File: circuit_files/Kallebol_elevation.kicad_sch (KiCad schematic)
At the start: 31 parts

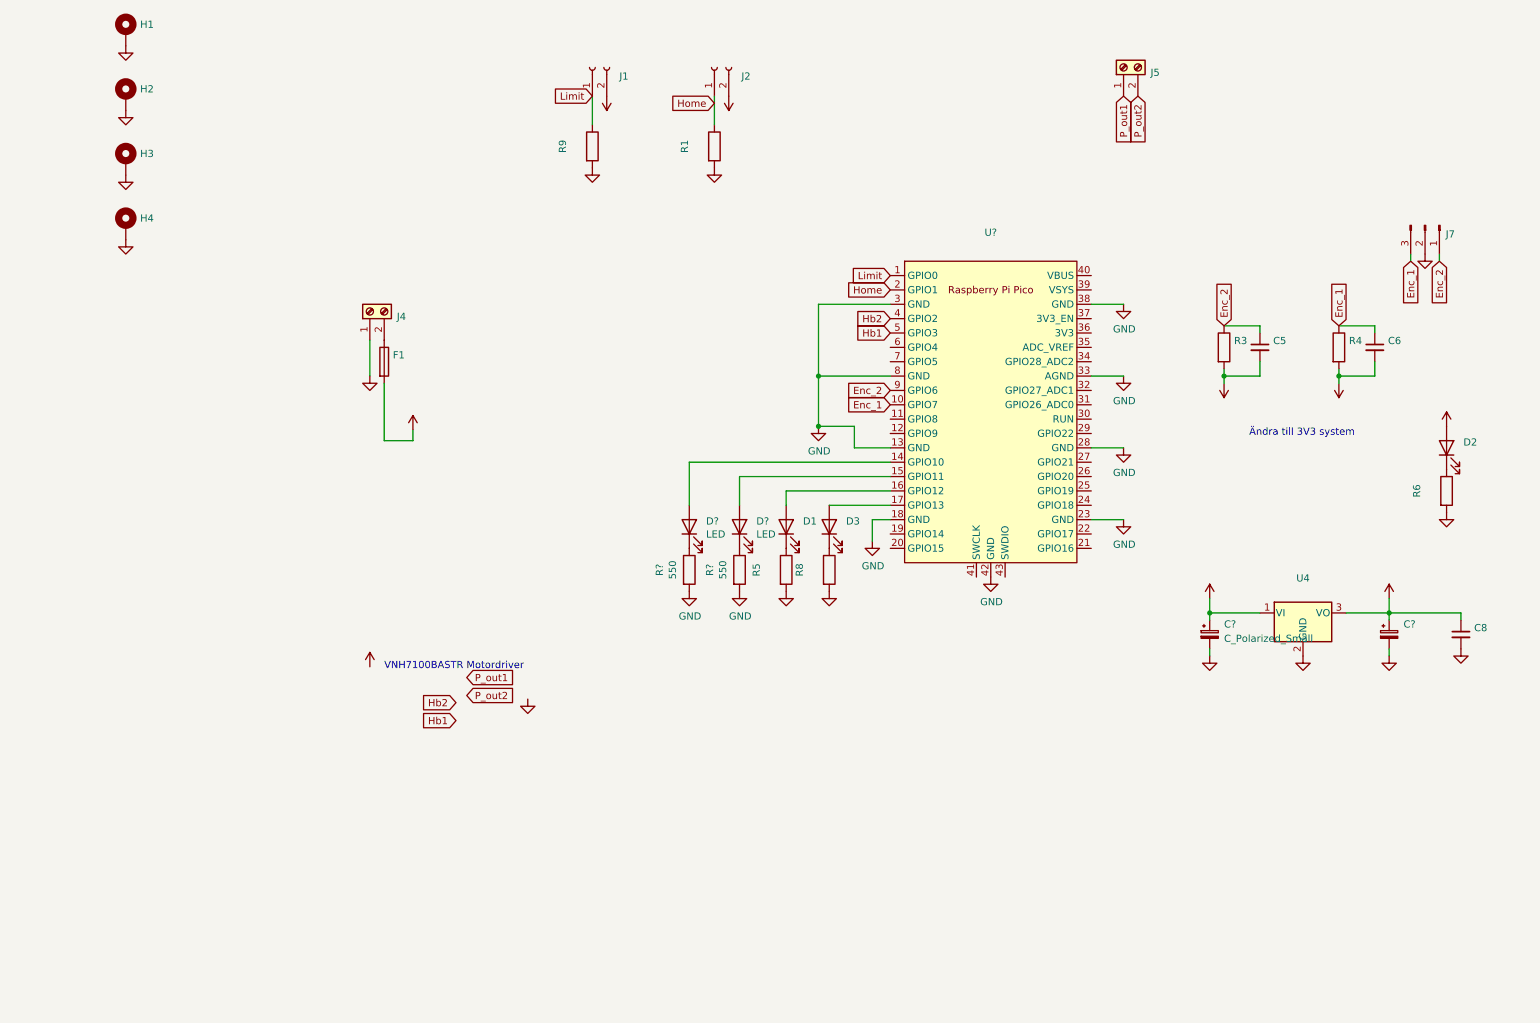
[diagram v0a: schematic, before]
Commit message: added basic driver circuit
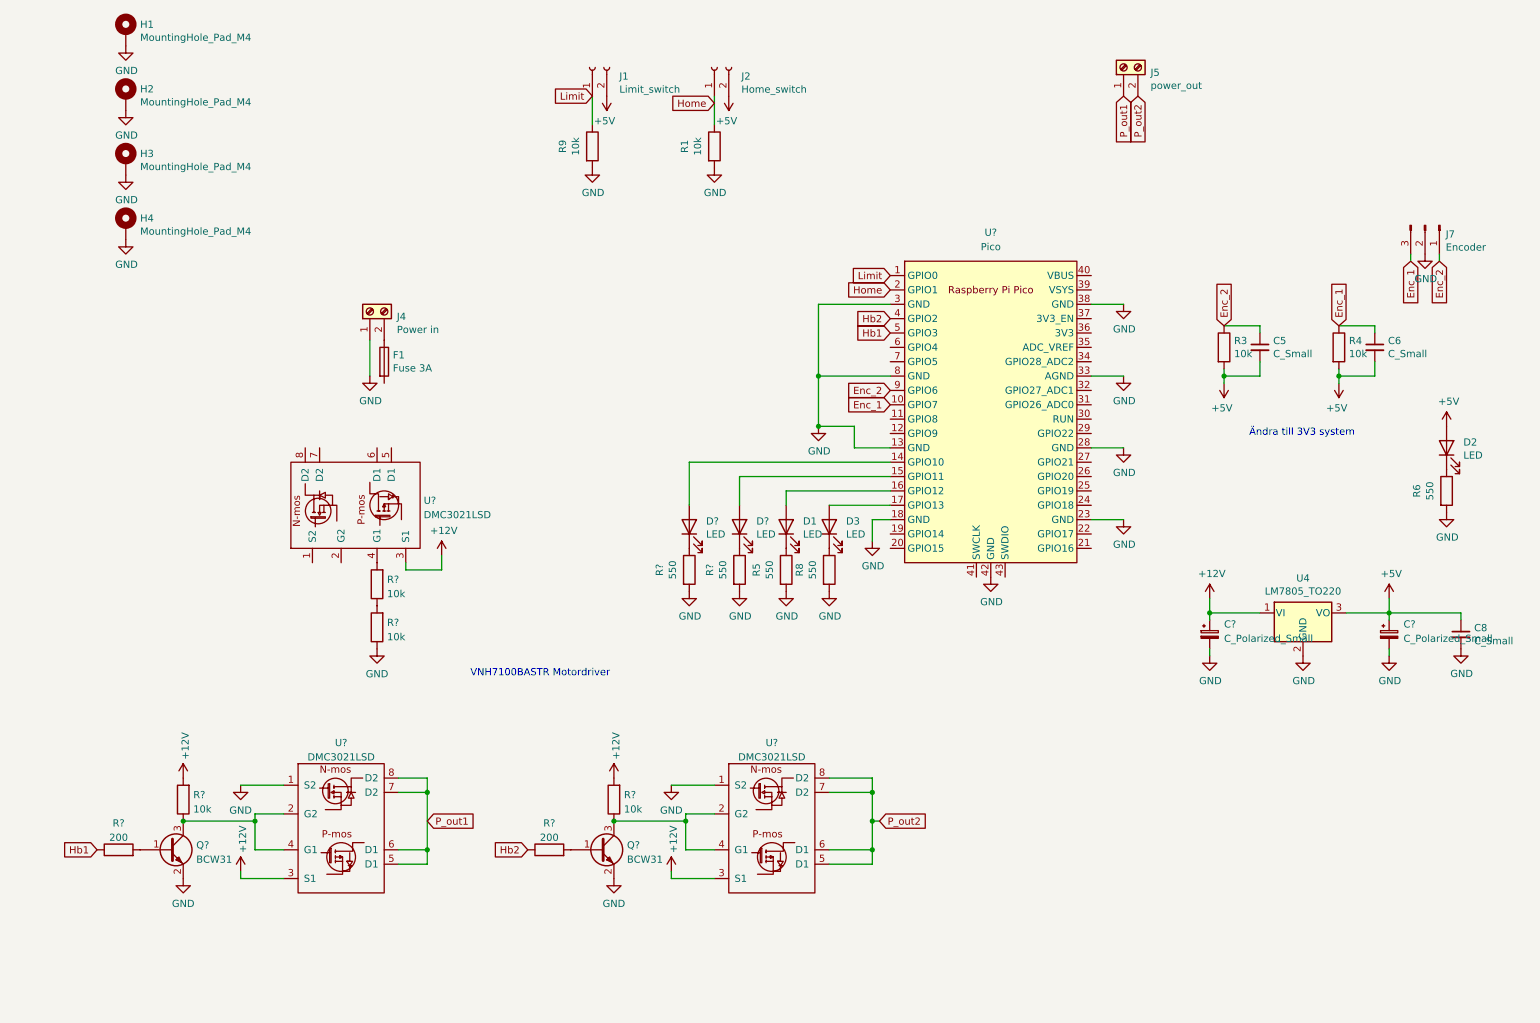
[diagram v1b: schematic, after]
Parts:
- added Q? (x2): BCW31, symbol Device:Q_NPN_BEC
- added R? (x2): 200, symbol Device:R
- added R? (x4): 10k, symbol Device:R
- added U? (x3): DMC3021LSD, Package_SO:SOIC-8_3.9x4.9mm_P1.27mm, symbol Kallebol_symLib:DMC3021LSD
- C5, C6, C8: value (none) -> C_Small; footprint (none) -> Capacitor_SMD:C_0603_1608Metric_Pad1.05x0.95mm_HandSolder
- C?: value (none) -> C_Polarized_Small
- D1, D2, D3: value (none) -> LED; footprint (none) -> LED_SMD:LED_0603_1608Metric
- F1: value (none) -> Fuse 3A; footprint (none) -> Xp_motor:Fuse_holder
- H1, H2, H3, H4: value (none) -> MountingHole_Pad_M4; footprint (none) -> MountingHole:MountingHole_4.3mm_M4_Pad
- J1: value (none) -> Limit_switch; footprint (none) -> TerminalBlock:TerminalBlock_bornier-2_P5.08mm
- J2: value (none) -> Home_switch; footprint (none) -> TerminalBlock:TerminalBlock_bornier-2_P5.08mm
- J4: value (none) -> Power in; footprint (none) -> TerminalBlock:TerminalBlock_bornier-2_P5.08mm
- J5: value (none) -> power_out; footprint (none) -> TerminalBlock:TerminalBlock_bornier-2_P5.08mm
- J7: value (none) -> Encoder; footprint (none) -> Connector_PinSocket_2.54mm:PinSocket_1x03_P2.54mm_Vertical
- R1, R3, R4, R9: value (none) -> 10k; footprint (none) -> Resistor_SMD:R_0603_1608Metric_Pad1.05x0.95mm_HandSolder
- R5, R6, R8: value (none) -> 550; footprint (none) -> Resistor_SMD:R_0603_1608Metric_Pad1.05x0.95mm_HandSolder
- U4: value (none) -> LM7805_TO220; footprint (none) -> Package_TO_SOT_THT:TO-220-3_Vertical
- U?: value (none) -> Pico; footprint (none) -> RPi_Pico:RPi_Pico_SMD_TH
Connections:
- net +12V: now also R?.2, R?.2, U?.3 (S1), U?.3 (S1), U?.3 (S1); no longer F1.2
- net GND: now also Q?.2 (E), Q?.2 (E), R?.1, U?.1 (S2), U?.1 (S2)
- net Hb1: now also R?.1
- net Hb2: now also R?.1
- net P_out1: now also U?.5 (D1), U?.6 (D1), U?.7 (D2), U?.8 (D2)
- net P_out2: now also U?.5 (D1), U?.6 (D1), U?.7 (D2), U?.8 (D2)
- new net: Q?.1 (B), R?.2 (x2)
- new net: Q?.3 (C), R?.1, U?.2 (G2), U?.4 (G1) (x2)
- new net: R?.1, R?.2
- new net: R?.2, U?.4 (G1)

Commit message: elevation part of the board functional
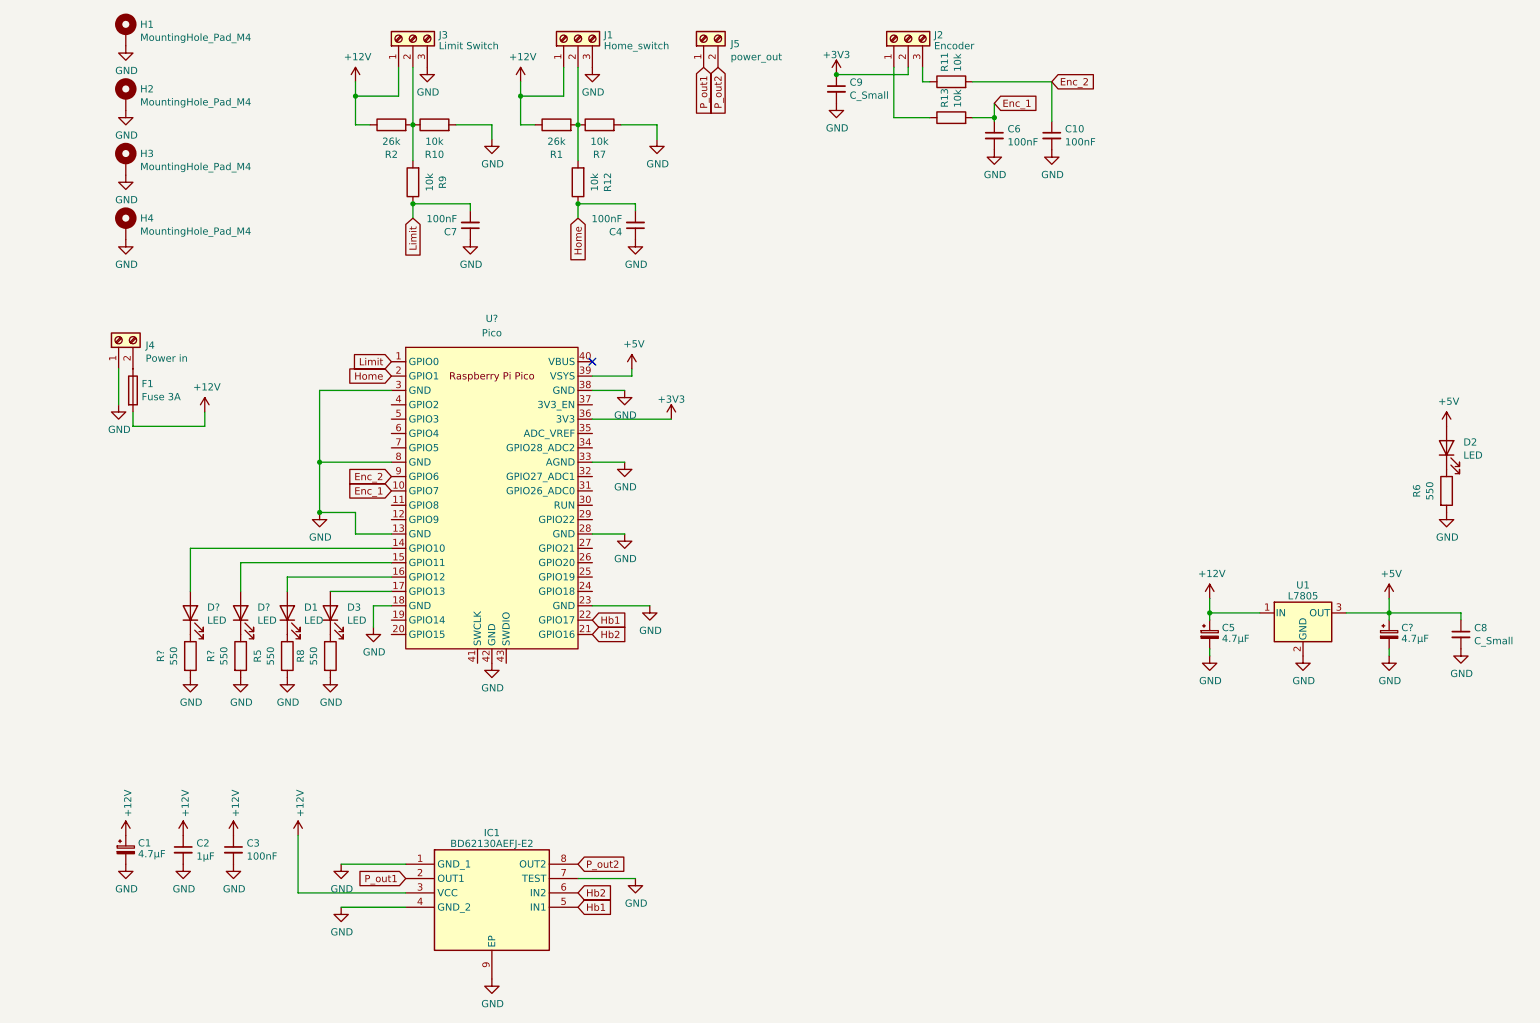
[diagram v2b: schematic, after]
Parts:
- removed C5: C_Small, Capacitor_SMD:C_0603_1608Metric_Pad1.05x0.95mm_HandSolder, symbol Device:C_Small
- removed C?: C_Polarized_Small, symbol Device:C_Polarized_Small
- removed J1: Limit_switch, TerminalBlock:TerminalBlock_bornier-2_P5.08mm, symbol Connector:Conn_01x02_Female
- removed J2: Home_switch, TerminalBlock:TerminalBlock_bornier-2_P5.08mm, symbol Connector:Conn_01x02_Female
- removed J7: Encoder, Connector_PinSocket_2.54mm:PinSocket_1x03_P2.54mm_Vertical, symbol Connector:Conn_01x03_Male
- removed Q? (x2): BCW31, symbol Device:Q_NPN_BEC
- removed R3, R4: 10k, Resistor_SMD:R_0603_1608Metric_Pad1.05x0.95mm_HandSolder, symbol Device:R
- removed R? (x2): 200, symbol Device:R
- removed R? (x4): 10k, symbol Device:R
- removed U4: LM7805_TO220, Package_TO_SOT_THT:TO-220-3_Vertical, symbol Regulator_Linear:LM7805_TO220
- removed U? (x3): DMC3021LSD, Package_SO:SOIC-8_3.9x4.9mm_P1.27mm, symbol Kallebol_symLib:DMC3021LSD
- added C1, C5: 4.7µF, symbol Device:C_Polarized_Small
- added C10, C3, C4, C7: 100nF, Capacitor_SMD:C_0603_1608Metric_Pad1.05x0.95mm_HandSolder, symbol Device:C_Small
- added C2: 1µF, Capacitor_SMD:C_0603_1608Metric_Pad1.05x0.95mm_HandSolder, symbol Device:C_Small
- added C9: C_Small, Capacitor_SMD:C_0603_1608Metric_Pad1.05x0.95mm_HandSolder, symbol Device:C_Small
- added IC1: BD62130AEFJ-E2, SOIC127P600X100-9N, symbol BD62130AEFJ-E2:BD62130AEFJ-E2
- added J1: Home_switch, symbol Connector:Screw_Terminal_01x03
- added J2: Encoder, symbol Connector:Screw_Terminal_01x03
- added J3: Limit Switch, symbol Connector:Screw_Terminal_01x03
- added R10, R11, R12, R13, R7: 10k, Resistor_SMD:R_0603_1608Metric_Pad1.05x0.95mm_HandSolder, symbol Device:R
- added R2: 26k, Resistor_SMD:R_0603_1608Metric_Pad1.05x0.95mm_HandSolder, symbol Device:R
- added U1: L7805, symbol Regulator_Linear:L7805
- C6: value C_Small -> 100nF
- C?: value C_Polarized_Small -> 4.7µF
- R1: value 10k -> 26k
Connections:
- net +12V: now also F1.2, R1.1, C1.1, C2.1, C3.1, C5.1, IC1.3 (VCC), J1.1 (Pin_1), J3.1 (Pin_1), R2.1, U1.1 (IN)
- net +5V: now also U?.39 (VSYS), U1.3 (OUT); no longer C6.2
- net Enc_1: now also R13.2
- net Enc_2: now also C10.1, R11.2
- net GND: now also C6.2, C1.2, C10.2, C2.2, C3.2, C4.1, C5.2, C7.1, C9.2, IC1.1 (GND_1), IC1.4 (GND_2), IC1.7 (TEST), IC1.9 (EP), J1.3 (Pin_3), J3.3 (Pin_3), R10.2, R7.2, U1.2 (GND); no longer R1.2, R9.2
- net Hb1: now also U?.22 (GPIO17), IC1.5 (IN1); no longer U?.5 (GPIO3)
- net Hb2: now also U?.21 (GPIO16), IC1.6 (IN2); no longer U?.4 (GPIO2)
- net Home: now also C4.2, R12.1; no longer R1.1
- net Limit: now also C7.2
- net P_out1: now also IC1.2 (OUT1)
- net P_out2: now also IC1.8 (OUT2)
- net +3V3: now reaches U?.36 (3V3)
- net +3V3: now also C9.1, J2.2 (Pin_2)
- new net: J2.1 (Pin_1), R13.1
- new net: J3.2 (Pin_2), R10.1, R2.2, R9.2
- new net: J2.3 (Pin_3), R11.1
- new net: J1.2 (Pin_2), R1.2, R12.2, R7.1
- no-connect marks 0 -> 1
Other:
- note removed: "VNH7100BASTR Motordriver"
- note removed: "Ändra till 3V3 system"
- moved on the sheet: D1, D3, D?, F1, J4, J5, R5, R8, R?, U?

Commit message: merged functionality with the GPIO fanout board
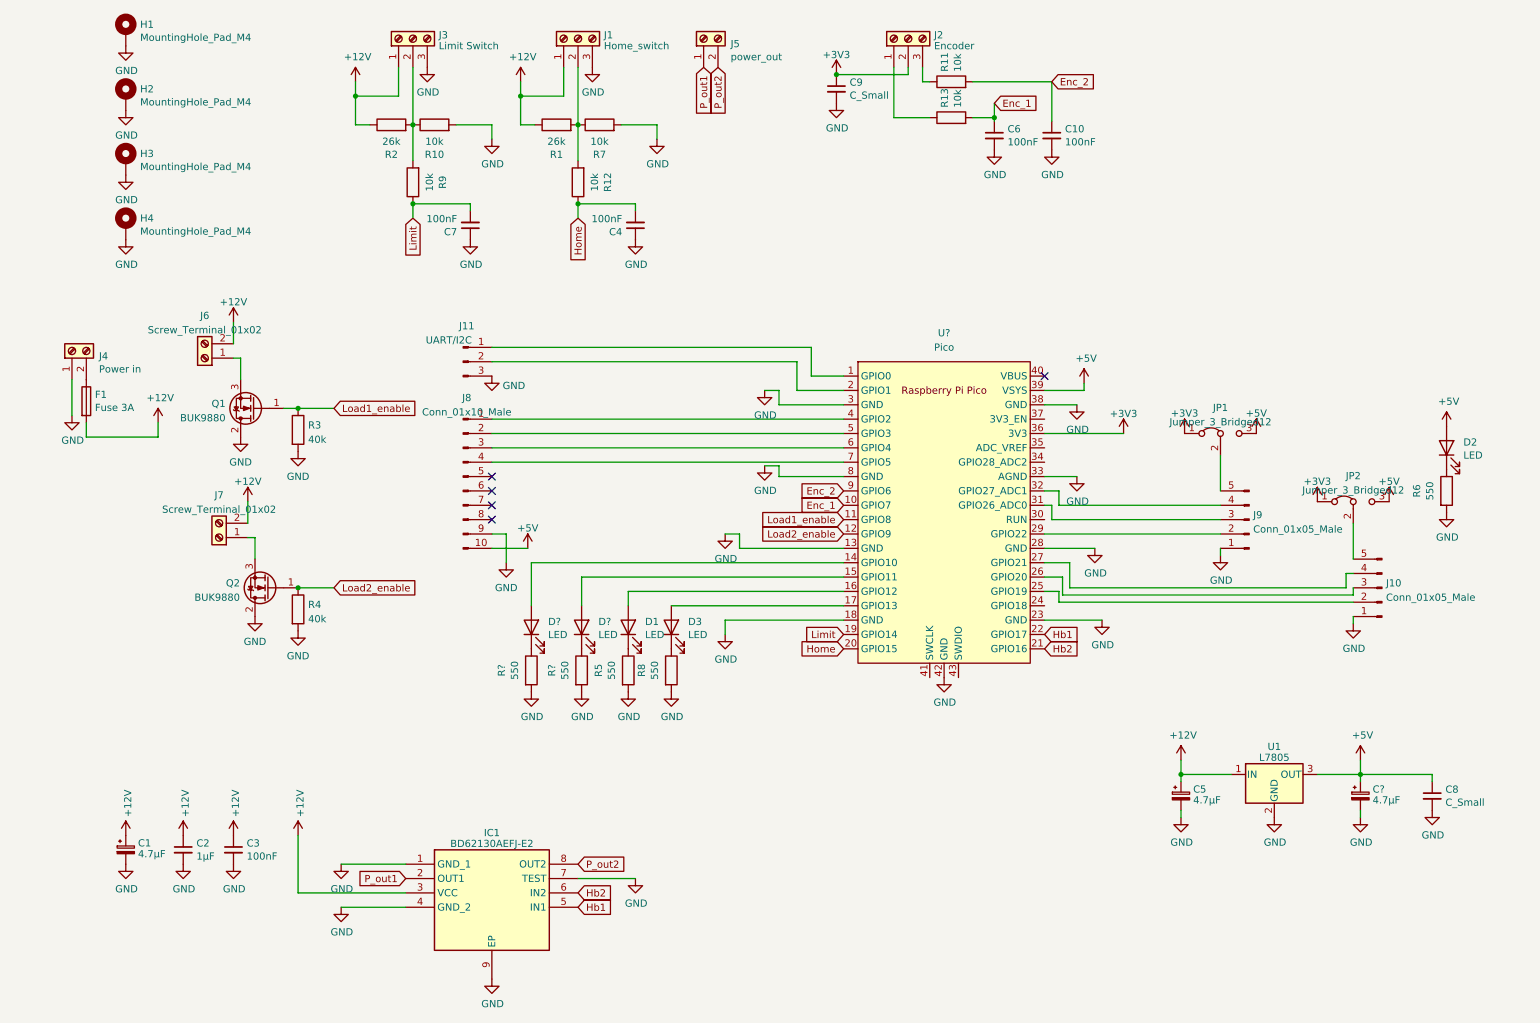
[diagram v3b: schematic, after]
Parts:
- added J10, J9: Conn_01x05_Male, Connector_PinSocket_2.54mm:PinSocket_1x05_P2.54mm_Vertical, symbol Connector:Conn_01x05_Male
- added J11: UART/I2C, Connector_PinSocket_2.54mm:PinSocket_1x03_P2.54mm_Vertical, symbol Connector:Conn_01x03_Male
- added J6, J7: Screw_Terminal_01x02, TerminalBlock:TerminalBlock_bornier-2_P5.08mm, symbol Connector:Screw_Terminal_01x02
- added J8: Conn_01x10_Male, Connector_PinSocket_2.54mm:PinSocket_1x10_P2.54mm_Vertical, symbol Connector:Conn_01x10_Male
- added JP1, JP2: Jumper_3_Bridged12, Connector_PinSocket_2.54mm:PinSocket_1x03_P2.54mm_Vertical, symbol Jumper:Jumper_3_Bridged12
- added Q1, Q2: BUK9880, Package_TO_SOT_SMD:SOT-223-3_TabPin2, symbol Device:Q_NMOS_GDS
- added R3, R4: 40k, Resistor_SMD:R_0603_1608Metric_Pad0.98x0.95mm_HandSolder, symbol Device:R
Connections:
- net +12V: now also J6.2 (Pin_2), J7.2 (Pin_2)
- net +3V3: now also JP1.1 (A), JP2.1 (A)
- net +5V: now also J8.10 (Pin_10), JP1.3 (B), JP2.3 (B)
- net GND: now also J10.1 (Pin_1), J11.3 (Pin_3), J8.9 (Pin_9), J9.1 (Pin_1), Q1.2 (D), Q2.2 (D), R3.2, R4.2
- net Home: now also U?.20 (GPIO15); no longer U?.2 (GPIO1)
- net Limit: now also U?.19 (GPIO14); no longer U?.1 (GPIO0)
- net Load1_enable: now reaches U?.11 (GPIO8)
- net Load1_enable: now also Q1.1 (G), R3.1
- net Load2_enable: now reaches U?.12 (GPIO9)
- net Load2_enable: now also Q2.1 (G), R4.1
- net at U?.25 (GPIO19): now also J10.2 (Pin_2)
- net at U?.26 (GPIO20): now also J10.3 (Pin_3)
- net at U?.27 (GPIO21): now also J10.4 (Pin_4)
- net at U?.29 (GPIO22): now also J9.2 (Pin_2)
- net at U?.31 (GPIO26_ADC0): now also J9.3 (Pin_3)
- net at U?.32 (GPIO27_ADC1): now also J9.4 (Pin_4)
- net at U?.4 (GPIO2): now also J8.1 (Pin_1)
- net at U?.5 (GPIO3): now also J8.2 (Pin_2)
- net at U?.6 (GPIO4): now also J8.3 (Pin_3)
- net at U?.7 (GPIO5): now also J8.4 (Pin_4)
- new net: J7.1 (Pin_1), Q2.3 (S)
- new net: J11.1 (Pin_1), U?.1 (GPIO0)
- new net: J11.2 (Pin_2), U?.2 (GPIO1)
- new net: J9.5 (Pin_5), JP1.2 (C)
- new net: J10.5 (Pin_5), JP2.2 (C)
- new net: J6.1 (Pin_1), Q1.3 (S)
- no-connect marks 1 -> 5
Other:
- moved on the sheet: C5, C8, C?, D1, D3, D?, F1, J4, R5, R8, R?, U1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

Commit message: sch seems done
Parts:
- added C11: C_Small, Capacitor_SMD:C_0603_1608Metric_Pad1.05x0.95mm_HandSolder, symbol Device:C_Small
- J8: value Conn_01x10_Male -> RF_switch
- JP1, JP2: value Jumper_3_Bridged12 -> Jumper_3
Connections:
- net +5V: now also C11.1
- net GND: now also C11.2
- no-connect marks 5 -> 12
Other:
- note added: "Haha, ser ut som en liten gubbe"
- moved on the sheet: C10, C5, C6, C8, C?, D2, F1, J10, J4, J6, J7, J9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
